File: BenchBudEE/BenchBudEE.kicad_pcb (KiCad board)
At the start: 4 copper layers, 165.1 x 63.5 mm, 125 parts, among them K1 1461069-5, P1 24 pin Mini-fit Jr, P2 CONN_3X2, P3 CONN_2, P4 12 pin terminal block, P5 3 Pin TB, Q1 2N3904, Q2 DMN65D8L-7, Q3 B130-13-F, Q4 B130-13-F, SW1 Power Switch, U1 LTV-816S, U10 MCP4801, U2 MCP3901, U3 LMT84, U4 OPA4170, U5 AP5726, U6 LM337T, U7 LM317, U8 LM317, U9 LM337T

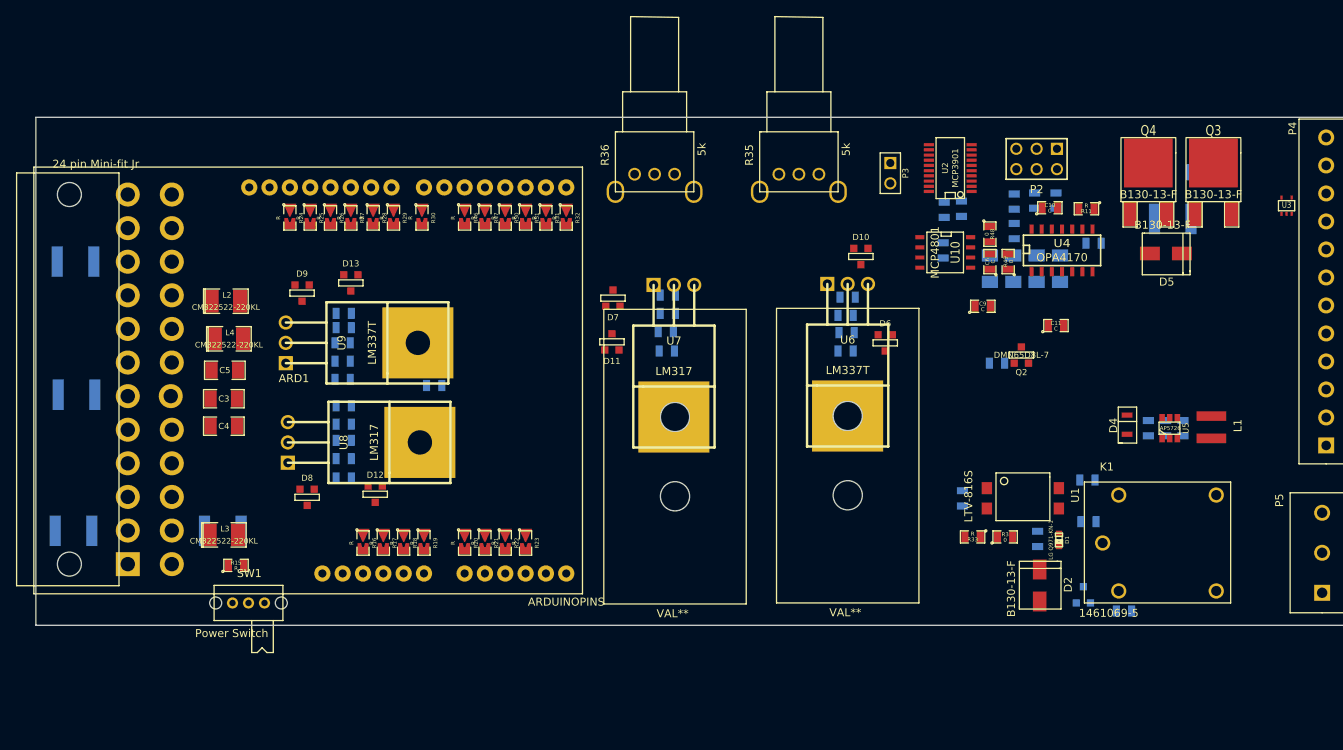
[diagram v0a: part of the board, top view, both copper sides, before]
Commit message: Ground and Power Planes
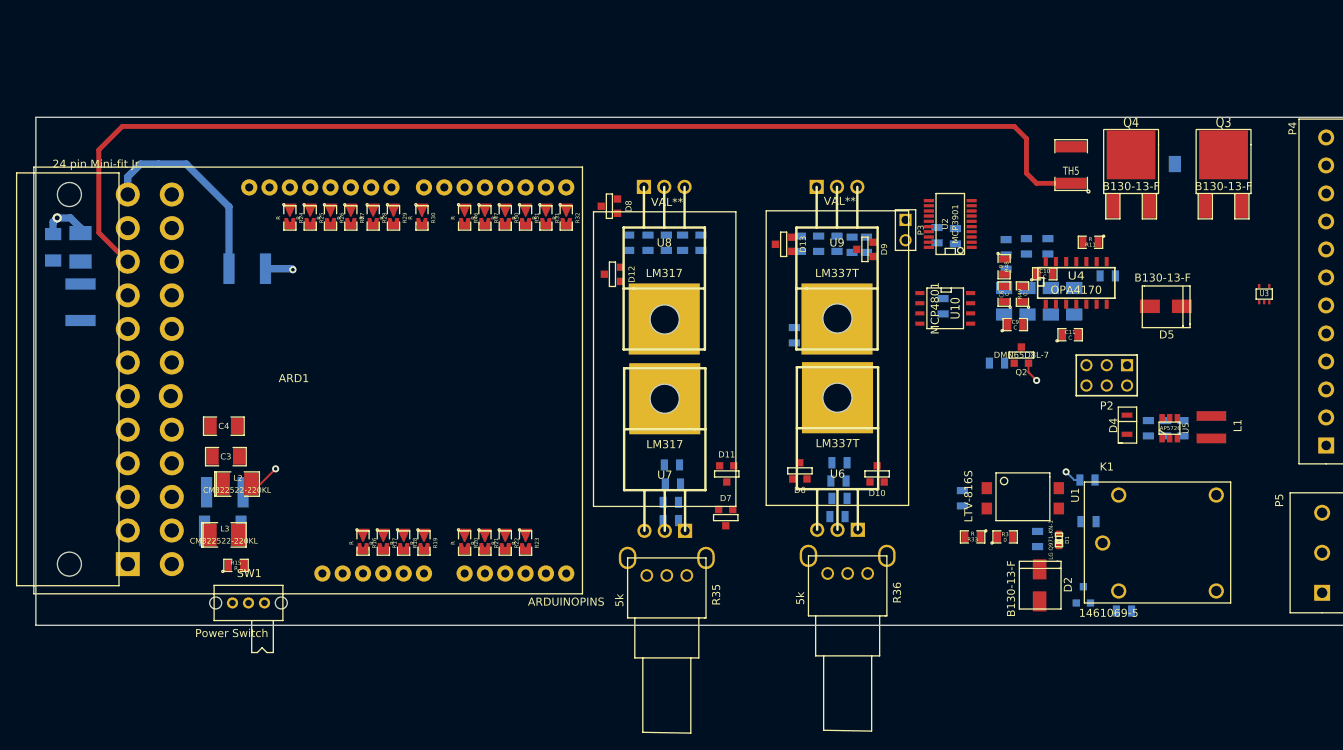
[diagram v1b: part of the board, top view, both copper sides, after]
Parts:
- C5, L4: moved to B.Cu
- TH5: moved to F.Cu
- moved U9 71.6 mm to (225.4, 106.7), turned to 270 degrees
- moved D9 70.6 mm to (228.9, 114.6), turned to 270 degrees
- moved C17 65.9 mm to (229.0, 114.0), turned to 90 degrees
- moved C24 64.4 mm to (227.3, 114.0), turned to 90 degrees
- moved R55 63.0 mm to (225.4, 113.9), turned to 270 degrees
- moved V2006B 62.2 mm to (234.3, 109.7), turned to 180 degrees
- moved R54 61.3 mm to (223.1, 113.9), turned to 270 degrees
- moved C21 59.7 mm to (220.8, 113.9), turned to 90 degrees
- moved U8 56.9 mm to (203.8, 106.7), turned to 270 degrees
- moved R36 55.4 mm to (226.7, 155.1), turned to 270 degrees
- moved D13 54.3 mm to (218.7, 113.9), turned to 270 degrees
- moved R35 52.8 mm to (204.1, 155.3), turned to 270 degrees
- moved D8 52.5 mm to (196.9, 109.2), turned to 270 degrees
- moved V2006B 49.2 mm to (212.7, 109.9), turned to 180 degrees
- moved C20 49.1 mm to (208.3, 113.7), turned to 270 degrees
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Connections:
- C1 pad 1: +5V -> +5P
- C10 pad 2: -12V -> FE_V-
- C11 pad 2: +12V -> FE_V+
- C13 pad 2: AGND -> GND
- L1 pad 1: +5V -> +5P
- P1 pad 12: (no net) -> N-00000115
- P1 pad 2: N-00000106 -> N-00000115
- P4 pad 1: +3.3V -> /LED_Driver/LED_STRING+
- P4 pad 10: /Fan/FAN_OUT- -> /Fan/TACH_IN
- P4 pad 11: /Thermocouple/TC IN + -> /Fan/FAN_OUT-
- P4 pad 12: /Thermocouple/TC IN - -> /Fan/FAN_OUT+
- P4 pad 2: +5V -> /LED_Driver/LED_STRING-
- P4 pad 6: /LED_Driver/LED_STRING+ -> +3.3V
- P4 pad 7: /LED_Driver/LED_STRING- -> +5V
- P4 pad 8: /Fan/TACH_IN -> /Thermocouple/TC IN +
- P4 pad 9: /Fan/FAN_OUT+ -> /Thermocouple/TC IN -
- Q3 pad 3: AGND -> GND
- R43 pad 2: AGND -> GND
- TH1 pad 1: N-00000106 -> N-00000115
- TH1 pad 2: (no net) -> +3.3V
- U4 pad 11: -12V -> FE_V-
- U4 pad 4: +12V -> FE_V+
- U5 pad 6: +5V -> +5P
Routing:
- net +12C: track 0.00 -> 143.7 mm
- net +3.3V: track 0.00 -> 139.9 mm, vias 0 -> 1
- net N-00000115: track 0.00 -> 25.5 mm
- net +5V: track 0.00 -> 6.32 mm, vias 0 -> 1
- net +12V: track 0.00 -> 3.84 mm, vias 0 -> 1
- net AGND: track 0.00 -> 2.58 mm, vias 0 -> 1
- net +12P: track 0.00 -> 2.14 mm, vias 0 -> 1
- added copper zone on PWR, net +12P
- added copper zone on PWR, net +12V
- added copper zone on PWR, net +5V
- added copper zone on PWR, net -12V
- added copper zone on GND, net AGND
- added copper zone on GND, net GND

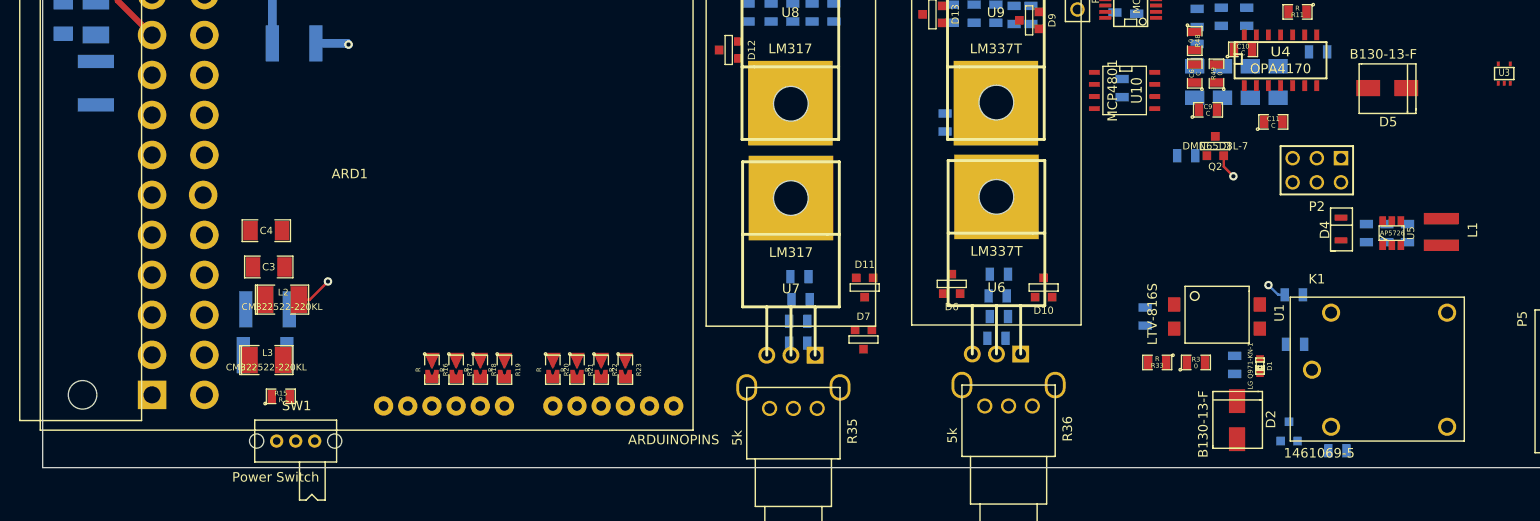
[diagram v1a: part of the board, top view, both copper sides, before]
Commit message: Ground and Power Planes (after saving)
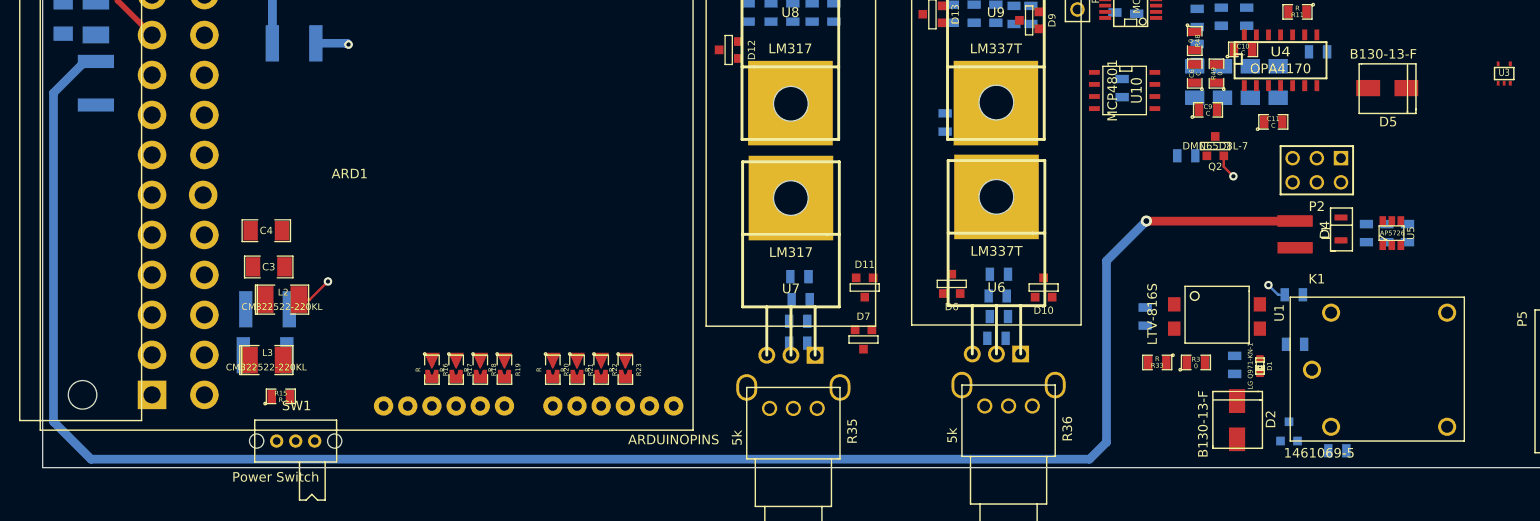
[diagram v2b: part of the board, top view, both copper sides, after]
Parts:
- moved L1 15.4 mm to (256.8, 135.6)
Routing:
- net +5P: track 0.00 -> 194.1 mm, vias 0 -> 1
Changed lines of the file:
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@@
   (general
     (links 326)
-    (no_connects 319)
+    (no_connects 318)
     (area 125.171999 97.993999 290.372001 161.594001)
     (thickness 1.6)
     (drawings 4)
-    (tracks 41)
+    (tracks 52)
     (zones 0)
     (modules 125)
@@
     (15 F.Cu signal)
     (2 PWR power)
-    (1 GND power hide)
+    (1 GND power)
     (0 B.Cu signal)
     (16 B.Adhes user)
@@
   )
   (module NR4012 (layer F.Cu)
-    (at 272.161 135.382 270)
+    (at 256.794 135.636 270)
     (fp_text reference L1 (at 1.2 -3.3 270) (layer F.SilkS)
       (effects (font (size 1 1) (thickness 0.15)))
@@
   (segment (start 236.093 116.84) (end 236.093 119.888) (width 0.9144) (layer PWR) (net 4))
   (segment (start 234.696 115.443) (end 236.093 116.84) (width 0.9144) (layer PWR) (net 4))
-  (segment (start 153.924 116.967) (end 157.226 116.967) (width 0.9144) (layer B.Cu) (net 4) (status 400000))
-  (segment (start 285.014 123.063) (end 286.512 121.565) (width 0.9144) (layer PWR) (net 4) (status 800000))
+  (segment (start 153.924 116.967) (end 157.226 116.967) (width 0.9144) (layer B.Cu) (net 4))
+  (segment (start 285.014 123.063) (end 286.512 121.565) (width 0.9144) (layer PWR) (net 4))
   (segment (start 236.093 119.888) (end 236.093 121.539) (width 0.9144) (layer PWR) (net 4))
   (segment (start 236.093 121.539) (end 237.617 123.063) (width 0.9144) (layer PWR) (net 4))
@@
   (via (at 157.353 117.094) (size 0.889) (layers F.Cu B.Cu) (net 4))
   (segment (start 157.226 116.967) (end 157.353 117.094) (width 0.9144) (layer B.Cu) (net 4))
-  (segment (start 130.81 112.522) (end 130.81 111.887) (width 0.9144) (layer B.Cu) (net 6) (status C00000))
+  (segment (start 241.173 135.636) (end 256.794 135.636) (width 0.9144) (layer F.Cu) (net 5) (status 800000))
+  (segment (start 130.81 118.872) (end 129.667 118.872) (width 0.9144) (layer B.Cu) (net 5))
+  (segment (start 241.173 135.636) (end 241.046 135.636) (width 0.9144) (layer F.Cu) (net 5))
+  (via (at 241.173 135.636) (size 1.1684) (drill 0.6096) (layers F.Cu B.Cu) (net 5))
+  (segment (start 236.982 139.827) (end 241.173 135.636) (width 0.9144) (layer B.Cu) (net 5))
+  (segment (start 236.982 158.877) (end 236.982 139.827) (width 0.9144) (layer B.Cu) (net 5))
+  (segment (start 235.204 160.655) (end 236.982 158.877) (width 0.9144) (layer B.Cu) (net 5))
+  (segment (start 130.302 160.655) (end 235.204 160.655) (width 0.9144) (layer B.Cu) (net 5))
+  (segment (start 126.365 156.718) (end 130.302 160.655) (width 0.9144) (layer B.Cu) (net 5))
+  (segment (start 126.365 122.174) (end 126.365 156.718) (width 0.9144) (layer B.Cu) (net 5))
+  (segment (start 129.667 118.872) (end 126.365 122.174) (width 0.9144) (layer B.Cu) (net 5))
+  (segment (start 130.81 112.522) (end 130.81 111.887) (width 0.9144) (layer B.Cu) (net 6))
   (segment (start 127.381 111.125) (end 127.889 110.617) (width 0.9144) (layer B.Cu) (net 6))
   (via (at 127.889 110.617) (size 1.1684) (drill 0.6096) (layers F.Cu B.Cu) (net 6))
-  (segment (start 127.381 111.125) (end 127.381 112.649) (width 0.9144) (layer B.Cu) (net 6) (status 800000))
+  (segment (start 127.381 111.125) (end 127.381 112.649) (width 0.9144) (layer B.Cu) (net 6))
   (segment (start 129.54 110.617) (end 127.889 110.617) (width 0.9144) (layer B.Cu) (net 6))
-  (segment (start 130.81 111.887) (end 129.54 110.617) (width 0.9144) (layer B.Cu) (net 6) (status 400000))
+  (segment (start 130.81 111.887) (end 129.54 110.617) (width 0.9144) (layer B.Cu) (net 6))
   (segment (start 249.301 128.778) (end 249.301 129.921) (width 0.254) (layer F.Cu) (net 42))
   (via (at 250.317 130.937) (size 0.889) (layers F.Cu B.Cu) (net 42))

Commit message: Reality Check
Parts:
- C9, R48: moved to B.Cu
- moved C9 31.7 mm to (278.6, 117.5), turned to 180 degrees
- moved R48 30.2 mm to (276.2, 120.3), turned to 90 degrees
- moved K1 1.09 mm to (257.9, 152.1)
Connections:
- K1 pad 3: /Relay/RELAY_NO -> /Relay/RELAY_NC
- K1 pad 4: /Relay/RELAY_NC -> /Relay/RELAY_NO
- P5 pad 1: /Relay/RELAY_NC -> /Relay/RELAY_NO
- P5 pad 3: /Relay/RELAY_NO -> /Relay/RELAY_NC
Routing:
- net +5P: track 194.1 -> 0.00 mm, vias 1 -> 0
- net +12C: track 143.7 -> 0.00 mm
- net +3.3V: track 139.9 -> 0.00 mm, vias 1 -> 0
- net N-00000115: track 25.5 -> 0.00 mm
- net +5V: track 6.32 -> 0.00 mm, vias 1 -> 0
- net +12V: track 3.84 -> 0.00 mm, vias 1 -> 0
- net AGND: track 2.58 -> 0.00 mm, vias 1 -> 0
- net +12P: track 2.14 -> 0.00 mm, vias 1 -> 0
- removed copper zone on PWR, net +12P
- removed copper zone on PWR, net +12V
- removed copper zone on PWR, net +5V
- removed copper zone on PWR, net -12V
- removed copper zone on GND, net AGND
- removed copper zone on GND, net GND

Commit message: Layout Work Session 1
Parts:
- removed V2006B (x2): VAL**, V2006B
- added 3 mm: VAL**, 3mm-NPTH, F.Cu at (140.0, 100.8)
- added 3 mm: VAL**, 3mm-NPTH, F.Cu at (139.8, 159.4)
- added 3 mm: VAL**, 3mm-NPTH, F.Cu at (279.0, 103.0)
- added JP1: JUMPER, PIN_ARRAY_2X1, F.Cu at (307.7, 186.4)
- U4: footprint SO14E -> SO14N
- U6, U7, U8, U9: footprint TO220 -> TO220_VERT
- moved C16 156.6 mm to (331.6, 197.5)
- moved R53 156.2 mm to (333.6, 197.5)
- moved R41 150.0 mm to (335.5, 197.5)
- moved R40 149.7 mm to (337.3, 197.5)
- moved D12 148.7 mm to (329.1, 186.7)
- moved C25 143.4 mm to (320.4, 197.5)
- moved R39 139.4 mm to (339.2, 197.5)
- moved D8 138.8 mm to (312.0, 186.7)
- moved C21 138.3 mm to (338.3, 186.8)
- moved C15 133.3 mm to (328.9, 196.6)
- moved D7 130.1 mm to (335.7, 186.7)
- moved R52 130.0 mm to (305.4, 197.5)
- moved D13 129.3 mm to (325.6, 186.7)
- moved D11 128.6 mm to (332.4, 186.7)
- moved C24 126.5 mm to (322.3, 197.5)
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
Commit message: Layout Work Session 2
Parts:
- TH5: moved to B.Cu
- moved C14 169.2 mm to (195.1, 76.2)
- moved C15 169.2 mm to (210.1, 76.2)
- moved C18 169.2 mm to (222.2, 65.5)
- moved C20 169.2 mm to (180.8, 77.1)
- moved C22 169.2 mm to (206.2, 76.2)
- moved C23 169.2 mm to (198.8, 76.2)
- moved C24 169.2 mm to (203.5, 77.1)
- moved D10 169.2 mm to (203.3, 66.3)
- moved D12 169.2 mm to (210.2, 66.3)
- moved D7 169.2 mm to (216.8, 66.3)
- moved D9 169.2 mm to (196.6, 66.3)
- moved JP1 169.2 mm to (188.8, 66.0)
- moved R34 169.2 mm to (183.6, 76.2)
- moved R37 169.2 mm to (180.0, 79.9)
- moved R40 169.2 mm to (218.4, 77.1)
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
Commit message: Layout Work Session 4
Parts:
- removed JP1: JUMPER, PIN_ARRAY_2X1
- added V8508H: VAL**, V8508H, F.Cu at (232.3, 100.3)
- added V8508H: VAL**, V8508H, F.Cu at (248.2, 100.5)
- moved R36 76.2 mm to (192.4, 101.1)
- moved R35 75.2 mm to (178.3, 101.5)
- moved U8 44.9 mm to (268.4, 100.6), turned to 270 degrees
- moved U9 33.8 mm to (268.6, 107.2), turned to 270 degrees
- moved U7 26.5 mm to (248.5, 107.3)
- moved U2 16.0 mm to (236.0, 118.5), turned to 180 degrees
- moved C3 13.6 mm to (170.1, 139.6)
- moved C4 13.6 mm to (169.8, 135.8)
- moved L3 13.6 mm to (169.8, 149.4)
- moved R15 13.6 mm to (171.3, 153.2)
- moved L2 13.6 mm to (171.4, 143.0)
- moved TH3 13.6 mm to (168.0, 144.3)
- moved TH4 13.6 mm to (168.0, 148.8)
- moved P2 9.16 mm to (252.6, 118.7)
- moved U6 7.36 mm to (232.7, 107.3)
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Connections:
- C1 pad 2: GND -> GND_LED
- C10 pad 1: AGND -> GND_TC
- C11 pad 1: AGND -> GND_TC
- C12 pad 1: AGND -> GND_FAN
- C13 pad 2: GND -> GND_FAN
- C14 pad 1: AGND -> GND_PWR
- C15 pad 2: AGND -> GND_PWR
- C16 pad 2: AGND -> GND_TC
- C17 pad 1: AGND -> GND_TC
- C18 pad 1: AGND -> GND_PWR
- C19 pad 2: AGND -> GND_PWR
- C2 pad 2: GND -> GND_LED
- C20 pad 2: AGND -> GND_TC
- C21 pad 1: AGND -> GND_TC
- C22 pad 1: AGND -> GND_PWR
- C23 pad 2: AGND -> GND_PWR
- C24 pad 1: AGND -> GND_TC
- C25 pad 2: AGND -> GND_TC
- C7 pad 1: AGND -> GND_TC
- C8 pad 2: AGND -> GND_TC
- C9 pad 2: AGND -> GND_TC
- D13 pad 2: AGND -> GND_TC
- P4 pad 10: /Fan/TACH_IN -> +3.3V
- P4 pad 11: /Fan/FAN_OUT- -> /PowerAdjustmentMonitor/V-_ADJ
- P4 pad 12: /Fan/FAN_OUT+ -> /PowerAdjustmentMonitor/V+_ADJ
- P4 pad 3: GND -> /Fan/TACH_IN
- P4 pad 4: /PowerAdjustmentMonitor/V+_ADJ -> /Fan/FAN_OUT-
- P4 pad 5: /PowerAdjustmentMonitor/V-_ADJ -> /Fan/FAN_OUT+
- P4 pad 6: +3.3V -> /Thermocouple/TC IN -
- P4 pad 7: +5V -> /Thermocouple/TC IN +
- P4 pad 8: /Thermocouple/TC IN + -> GND
- P4 pad 9: /Thermocouple/TC IN - -> +5V
- Q2 pad S: AGND -> GND_FAN
- Q3 pad 3: GND -> GND_FAN
- R14 pad 2: GND -> GND_LED
- R2 pad 2: GND -> GND_RELAY
- R35 pad 1: AGND -> GND_PWR
- R36 pad 2: AGND -> (no net)
- R39 pad 1: AGND -> GND_PWR
- R40 pad 2: AGND -> GND_PWR
- R43 pad 2: GND -> GND_FAN
- R48 pad 1: AGND -> GND_TC
- R49 pad 1: AGND -> GND_TC
- R53 pad 1: AGND -> GND_TC
- R54 pad 2: AGND -> GND_TC
- R6 pad 2: GND -> GND_RELAY
- R8 pad 1: AGND -> GND_TC
- U10 pad 7: AGND -> GND_FAN
- U2 pad 11: AGND -> GND_TC
- U2 pad 8: AGND -> GND_TC
- U3 pad 1: AGND -> GND_TC
- U3 pad 2: AGND -> GND_TC
- U3 pad 5: AGND -> GND_TC
- U5 pad 2: GND -> GND_LED
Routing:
- net GND_FAN: track 0.00 -> 2.76 mm, vias 0 -> 1
- net GND_LED: track 0.00 -> 2.60 mm, vias 0 -> 1
- net GND_RELAY: track 0.00 -> 2.16 mm, vias 0 -> 1
- net GND_TC: track 0.00 -> 1.80 mm, vias 0 -> 1
- added copper zone on GND, net GND_FAN
- added copper zone on GND, net GND_LED
- added copper zone on GND, net GND_PWR
- added copper zone on GND, net GND_RELAY
- added copper zone on GND, net GND_TC

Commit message: Layout Work Session 5
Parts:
- added TP1: CONN_1, 1pin, F.Cu at (160.8, 133.9)
- moved L3 48.4 mm to (149.7, 105.3), turned to 180 degrees
- moved L2 39.0 mm to (149.7, 110.6)
- moved C4 35.5 mm to (155.3, 103.4), turned to 270 degrees
- moved C3 30.8 mm to (155.3, 112.5), turned to 270 degrees
- moved TH3 22.2 mm to (148.7, 155.2), turned to 0 degrees
- moved TH4 19.5 mm to (148.6, 149.7)
- moved U8 13.6 mm to (259.0, 110.4)
- moved 3 mm 10.4 mm to (129.5, 100.6)
- moved 3 mm 10.4 mm to (129.4, 159.3)
- moved C5 9.02 mm to (118.4, 114.4)
- moved L4 9.02 mm to (121.8, 114.4)
- moved TH2 9.02 mm to (121.8, 121.3)
- moved R36 7.75 mm to (200.2, 101.0)
- moved D5 7.28 mm to (276.5, 119.0)
- moved Q3 6.99 mm to (277.1, 129.3)
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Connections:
- C10 pad 1: GND_TC -> AGND
- C11 pad 1: GND_TC -> AGND
- C12 pad 1: GND_FAN -> AGND
- C13 pad 2: GND_FAN -> AGND
- C16 pad 2: GND_TC -> AGND
- C17 pad 1: GND_TC -> AGND
- C18 pad 2: N-00000127 (its old number) -> N-00000125
- C20 pad 2: GND_TC -> AGND
- C21 pad 1: GND_TC -> AGND
- C24 pad 1: GND_TC -> AGND
- C25 pad 2: GND_TC -> AGND
- C7 pad 1: GND_TC -> AGND
- C8 pad 2: GND_TC -> AGND
- C9 pad 2: GND_TC -> AGND
- D10 pad 2: N-00000127 (its old number) -> N-00000125
- D13 pad 2: GND_TC -> AGND
- P4 pad 8: GND -> GND_PWR
- Q2 pad S: GND_FAN -> AGND
- Q3 pad 3: GND_FAN -> AGND
- R34 pad 2: N-00000127 (its old number) -> N-00000125
- R35 pad 1: GND_PWR -> N-00000125
- R35 pad 2: N-00000127 (its old number) -> GND_PWR
- R36 pad 2: (no net) -> GND_PWR
- R43 pad 2: GND_FAN -> AGND
- R48 pad 1: GND_TC -> AGND
- R49 pad 1: GND_TC -> AGND
- R53 pad 1: GND_TC -> AGND
- R54 pad 2: GND_TC -> AGND
- R8 pad 1: GND_TC -> AGND
- U10 pad 7: GND_FAN -> AGND
- U2 pad 11: GND_TC -> AGND
- U2 pad 8: GND_TC -> AGND
- U3 pad 1: GND_TC -> AGND
- U3 pad 2: GND_TC -> AGND
- U3 pad 5: GND_TC -> AGND
- U6 pad 1: N-00000127 (its old number) -> N-00000125
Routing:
- net +12V: track 0.00 -> 195.7 mm, vias 0 -> 1
- net -12V: track 0.00 -> 193.9 mm, vias 0 -> 1
- net +12C: track 0.00 -> 189.0 mm, vias 0 -> 2
- net /Relay/RELAY_COM: track 0.00 -> 21.9 mm
- net /Relay/RELAY_NO: track 0.00 -> 8.06 mm
- net /Relay/RELAY_NC: track 0.00 -> 7.29 mm
- net GND_FAN: track 2.76 -> 0.00 mm, vias 1 -> 0
- net +5V: track 0.00 -> 2.61 mm, vias 0 -> 1
- net +5P: track 0.00 -> 2.24 mm, vias 0 -> 1
- net AGND: track 0.00 -> 2.04 mm, vias 0 -> 1
- net +12P: track 0.00 -> 1.97 mm, vias 0 -> 1
- net GND_TC: track 1.80 -> 0.00 mm, vias 1 -> 0
- net GND_LED: track 2.60 -> 1.96 mm
- added copper zone on PWR, net +12P
- added copper zone on PWR, net +5P
- added copper zone on PWR, net +5V
- added copper zone on GND, net AGND
- removed copper zone on GND, net GND_FAN
- removed copper zone on GND, net GND_TC
